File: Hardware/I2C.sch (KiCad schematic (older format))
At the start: 8 parts, among them J16 I2C 5V, J17 PPS, J6 I2C 3.3V, J8 I2C 3.3V, U4 BSS138, U5 BSS138

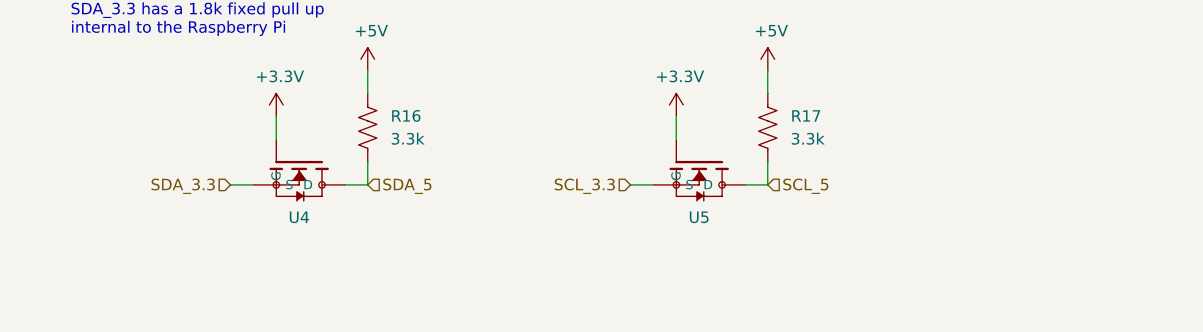
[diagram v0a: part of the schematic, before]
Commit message: Organized Schematic Naming and Added Comments
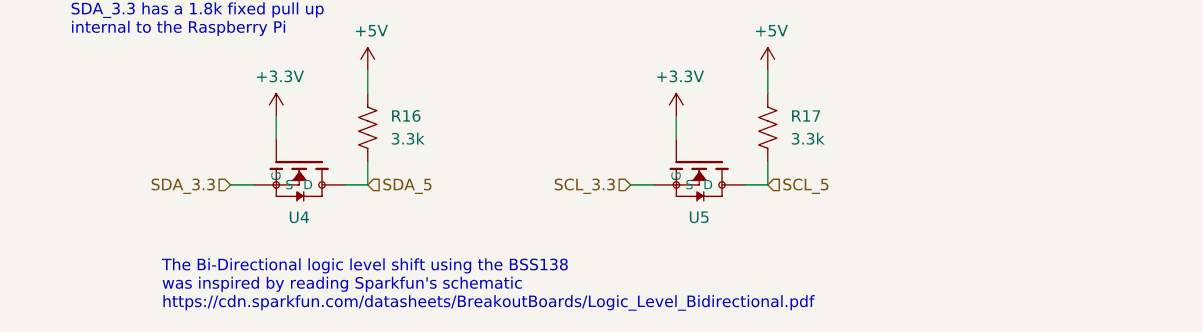
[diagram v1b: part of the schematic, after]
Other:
- note added: "The Bi-Directional logic level shift using the BSS138\nwas inspired by reading Sparkfun's schematic\nhttps://cdn.sparkfun.com/datasheets/BreakoutBoards/Logic_Level_Bidirectional.pdf"
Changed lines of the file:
@@
 EESchema Schematic File Version 4
-LIBS:rpi-hat-cache
+LIBS:TopLevel-cache
 EELAYER 30 0
 EELAYER END
@@
 Sheet 6 7
 Title ""
-Date ""
+Date "2019-11-15"
 Rev ""
-Comp ""
+Comp "Zephyrus, Indoor Air Quality - Raspberry Pi HAT"
 Comment1 ""
 Comment2 ""
@@
 Text Notes 4950 1500 0    118  ~ 24
 I2C Sensors/Connectors
+Text Notes 4450 5450 0    50   ~ 0
+The Bi-Directional logic level shift using the BSS138\nwas inspired by reading Sparkfun's schematic\nhttps://cdn.sparkfun.com/datasheets/BreakoutBoards/Logic_Level_Bidirectional.pdf
 $EndSCHEMATC

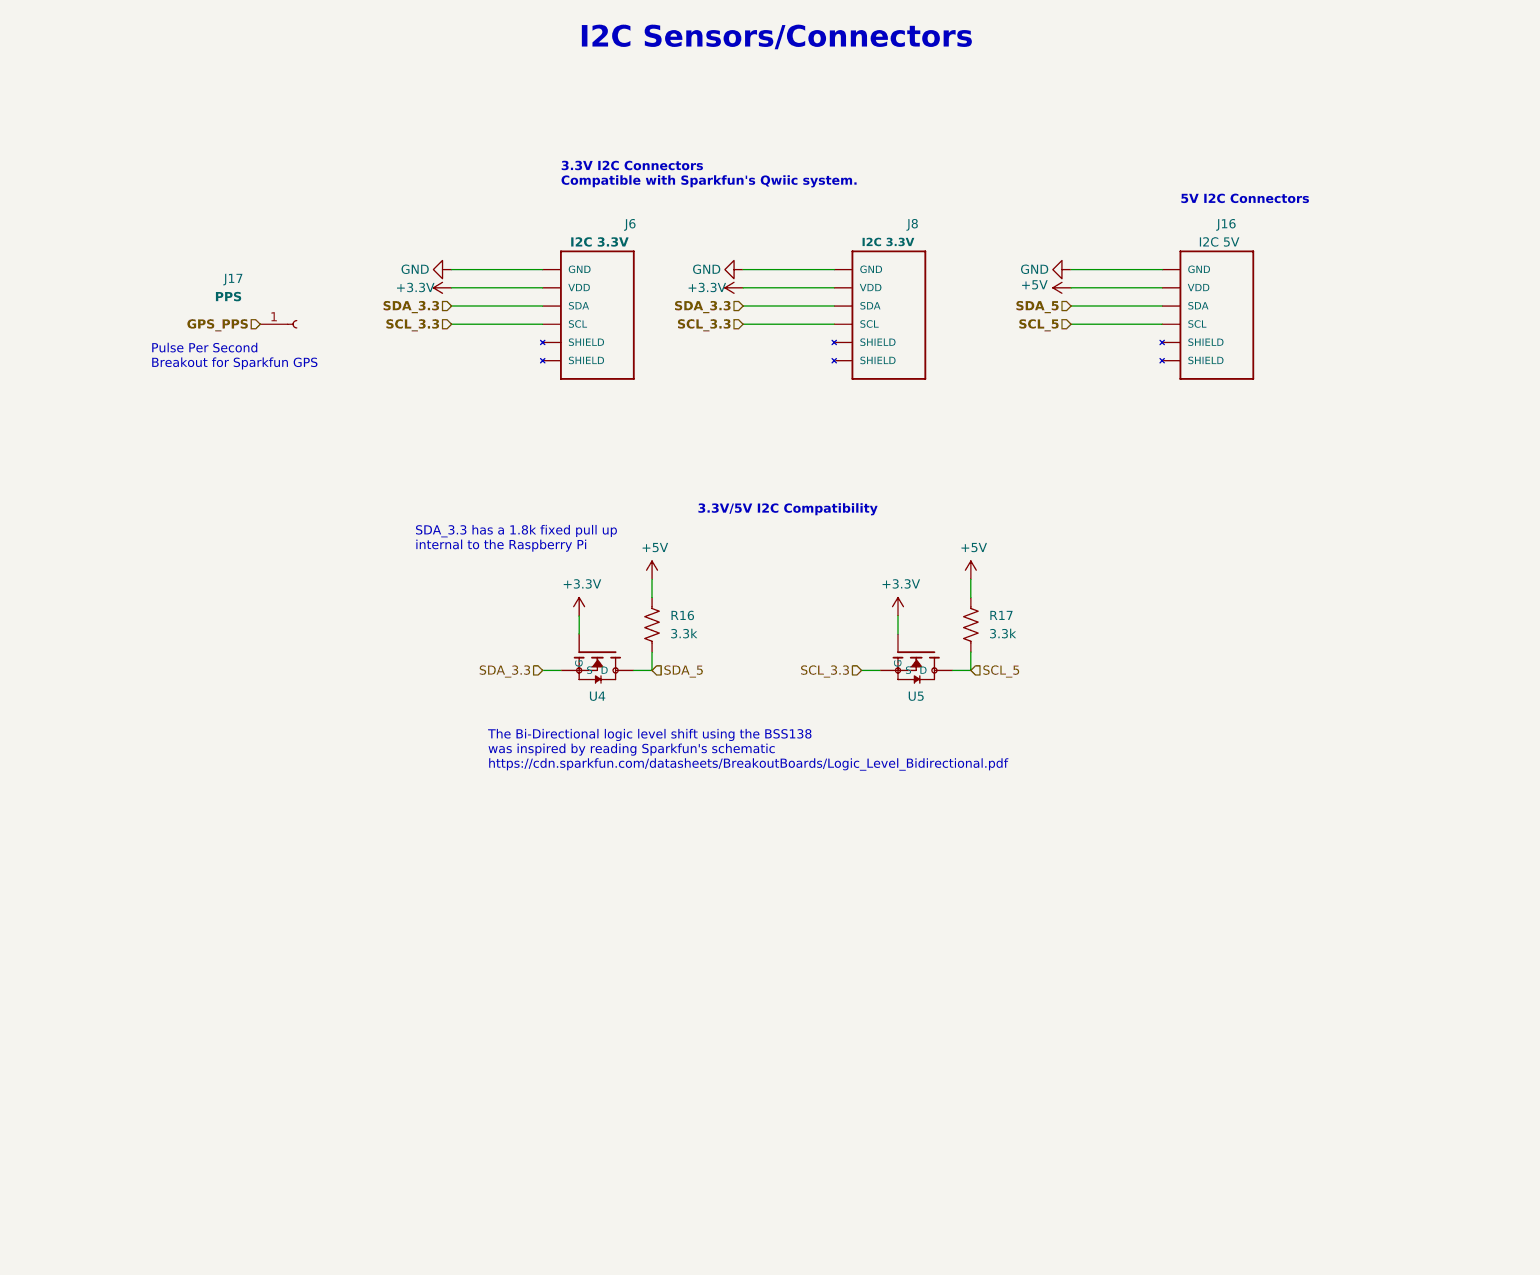
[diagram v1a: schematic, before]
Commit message: Up Changed I2C addres for DAC and ADC.  Added MOSFET to USART RX.
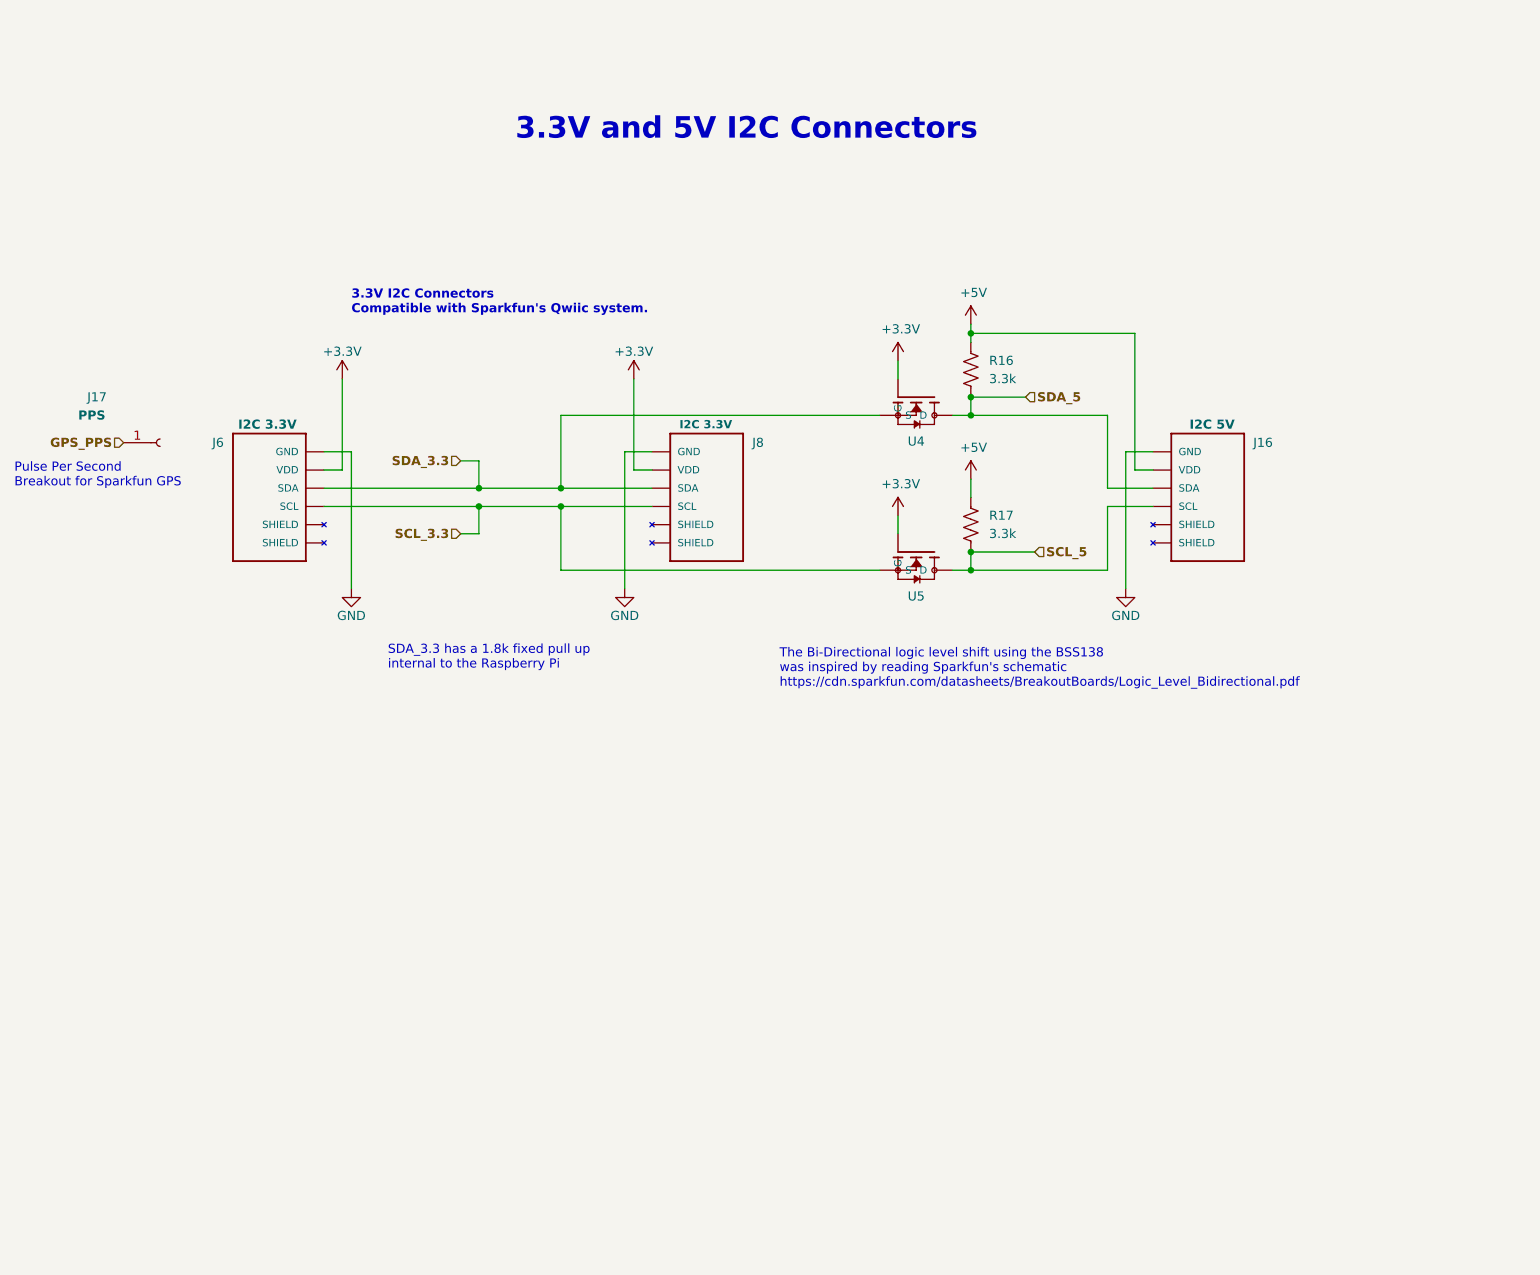
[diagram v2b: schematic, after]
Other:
- note added: "3.3V and 5V I2C Connectors"
- note removed: "3.3V/5V I2C Compatibility"
- note removed: "5V I2C Connectors\n"
- note removed: "I2C Sensors/Connectors"
- moved on the sheet: J16, J17, J6, J8, R16, R17, U4, U5

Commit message: Updated Schematic Attribution and Documentation
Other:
- note added: "The Bi-Directional logic level shift using the BSS138\nwas inspired by reading Sparkfun's schematic\nhttps://cdn.sparkfun.com/datasheets/BreakoutBoards/Logic_Level_Bidirectional.pdf\n\nLicense:\nhttps://creativecommons.org/licenses/by-sa/3.0/us/\n\nChanges:\nThere is no Pull-Up on the Source, because of the\ninterl Raspberry Pi 1.8k Pull-Ups"
- note removed: "SDA_3.3 has a 1.8k fixed pull up\ninternal to the Raspberry Pi"
- note removed: "The Bi-Directional logic level shift using the BSS138\nwas inspired by reading Sparkfun's schematic\nhttps://cdn.sparkfun.com/datasheets/BreakoutBoards/Logic_Level_Bidirectional.pdf"
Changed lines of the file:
@@
 EESchema Schematic File Version 4
+LIBS:Zephyrus-IAQ-HAT-cache
 EELAYER 30 0
 EELAYER END
-$Descr A4 11693 8268
+$Descr USLetter 11000 8500
 encoding utf-8
-Sheet 6 7
+Sheet 5 7
 Title "I2C Connectors and Logic Level Conversion"
 Date "2019-11-15"
@@
 Wire Wire Line
 	6700 3200 6700 3300
-Text Notes 3900 4900 0    50   ~ 0
-SDA_3.3 has a 1.8k fixed pull up\ninternal to the Raspberry Pi
 Wire Wire Line
 	6700 4050 6700 4150
 Text Notes 4600 2000 0    118  ~ 24
 3.3V and 5V I2C Connectors
-Text Notes 6050 5000 0    50   ~ 0
-The Bi-Directional logic level shift using the BSS138\nwas inspired by reading Sparkfun's schematic\nhttps://cdn.sparkfun.com/datasheets/BreakoutBoards/Logic_Level_Bidirectional.pdf
+Text Notes 6300 5550 0    50   ~ 0
+The Bi-Directional logic level shift using the BSS138\nwas inspired by reading Sparkfun's schematic\nhttps://cdn.sparkfun.com/datasheets/BreakoutBoards/Logic_Level_Bidirectional.pdf\n\nLicense:\nhttps://creativecommons.org/licenses/by-sa/3.0/us/\n\nChanges:\nThere is no Pull-Up on the Source, because of the\ninterl Raspberry Pi 1.8k Pull-Ups
 Connection ~ 7100 3050
 Wire Wire Line
@@
 Wire Wire Line
 	7100 3500 7850 3500
+$Comp
+L cc-by-sa:LOGO #G5
+U 1 1 5DD3A469
+P 5350 7550
+F 0 "#G5" H 5350 7287 60  0001 C CNN
+F 1 "LOGO" H 5350 7813 60  0001 C CNN
+F 2 "" H 5350 7550 50  0001 C CNN
+F 3 "" H 5350 7550 50  0001 C CNN
+	1    5350 7550
+	1    0    0    -1
+$EndComp
 $EndSCHEMATC
